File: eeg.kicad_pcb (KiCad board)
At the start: 2 copper layers, 155 parts, among them J1 USB_B_Mini, U1 STM32F446RE, U10 -.+2.5V.+3.3V-GND, U11 +5V, U12 RN4678-V_RM100, U13 ADS1299IPAG, U2 ADS1299-8CHANNEL, U3 LD39050PU33R, U4 TPS60403DBVT, U5 TPS73225DBVT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

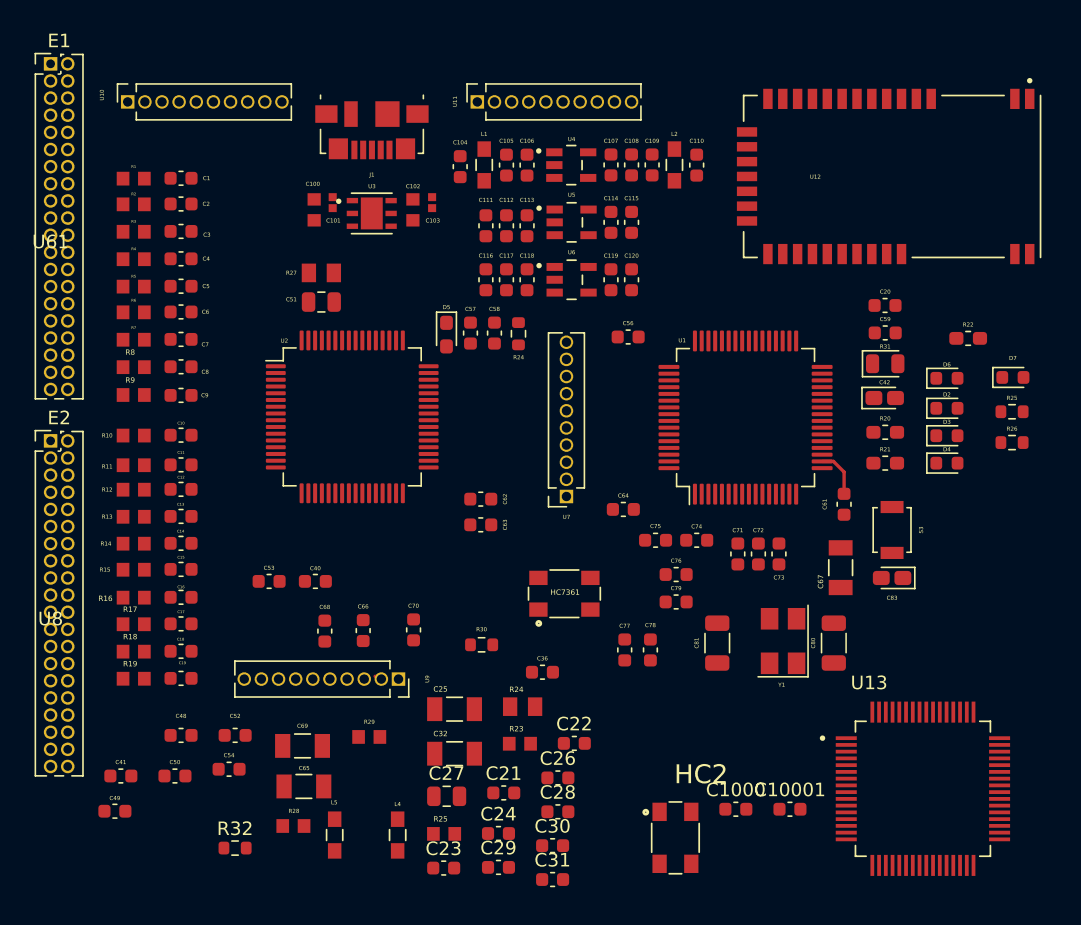
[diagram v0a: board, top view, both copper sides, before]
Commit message: RC connections realigned
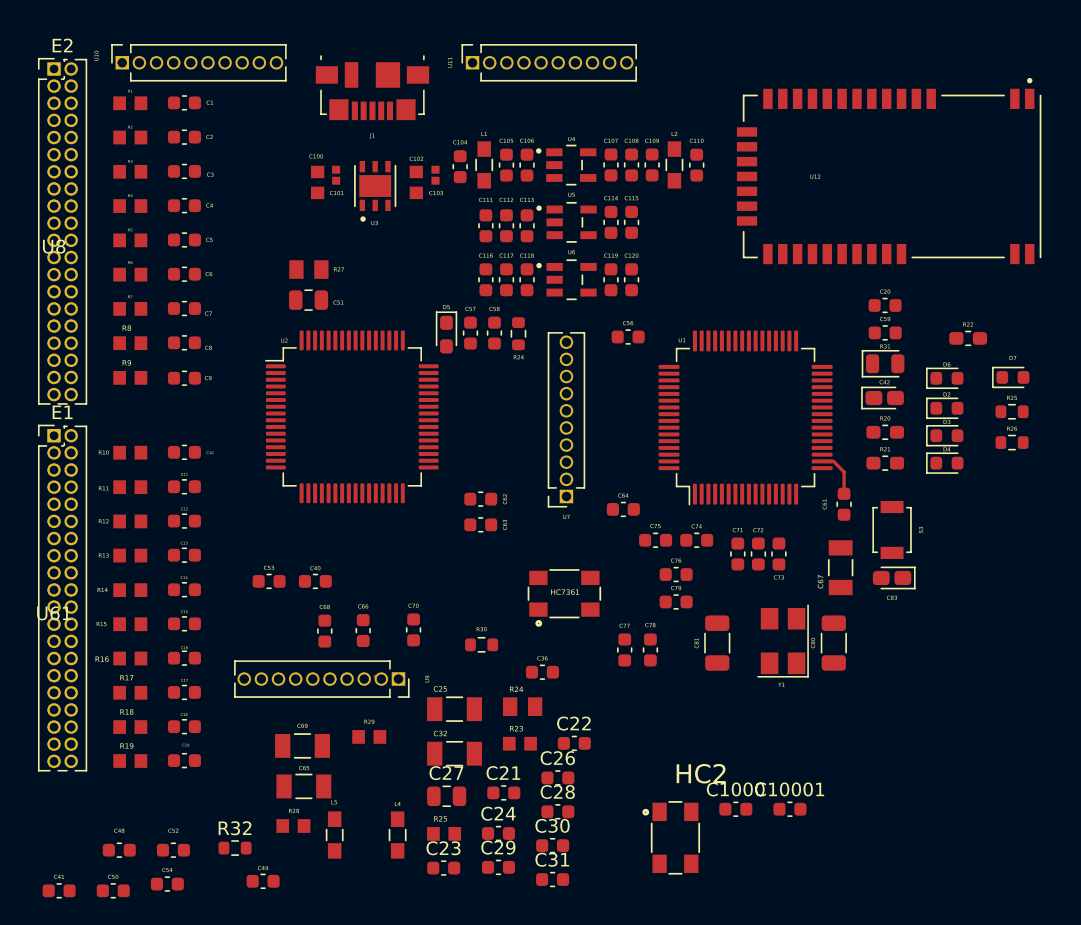
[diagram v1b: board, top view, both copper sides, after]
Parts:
- removed U13: ADS1299IPAG, QFP50P1200X1200X120-64N
- moved U61 27.6 mm to (39.8, 71.6)
- moved U8 27.6 mm to (39.8, 44.5)
- moved C49 12.1 mm to (55.2, 91.9)
- moved C50 9.66 mm to (44.1, 92.7)
- moved C52 9.66 mm to (48.6, 89.6)
- moved C54 9.66 mm to (48.2, 92.2)
- moved C41 9.66 mm to (40.1, 92.7)
- moved C48 9.66 mm to (44.6, 89.6)
- moved R19 6.10 mm to (45.4, 83.0)
- moved C19 6.10 mm to (49.4, 83.0)
- moved C1 5.59 mm to (49.4, 34.3)
- moved R1 5.59 mm to (45.4, 34.3)
- moved C18 5.59 mm to (49.4, 80.5)
- moved R18 5.59 mm to (45.4, 80.5)
- moved C17 5.09 mm to (49.4, 78.0)
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
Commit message: ADS1299 Tracks fixed.
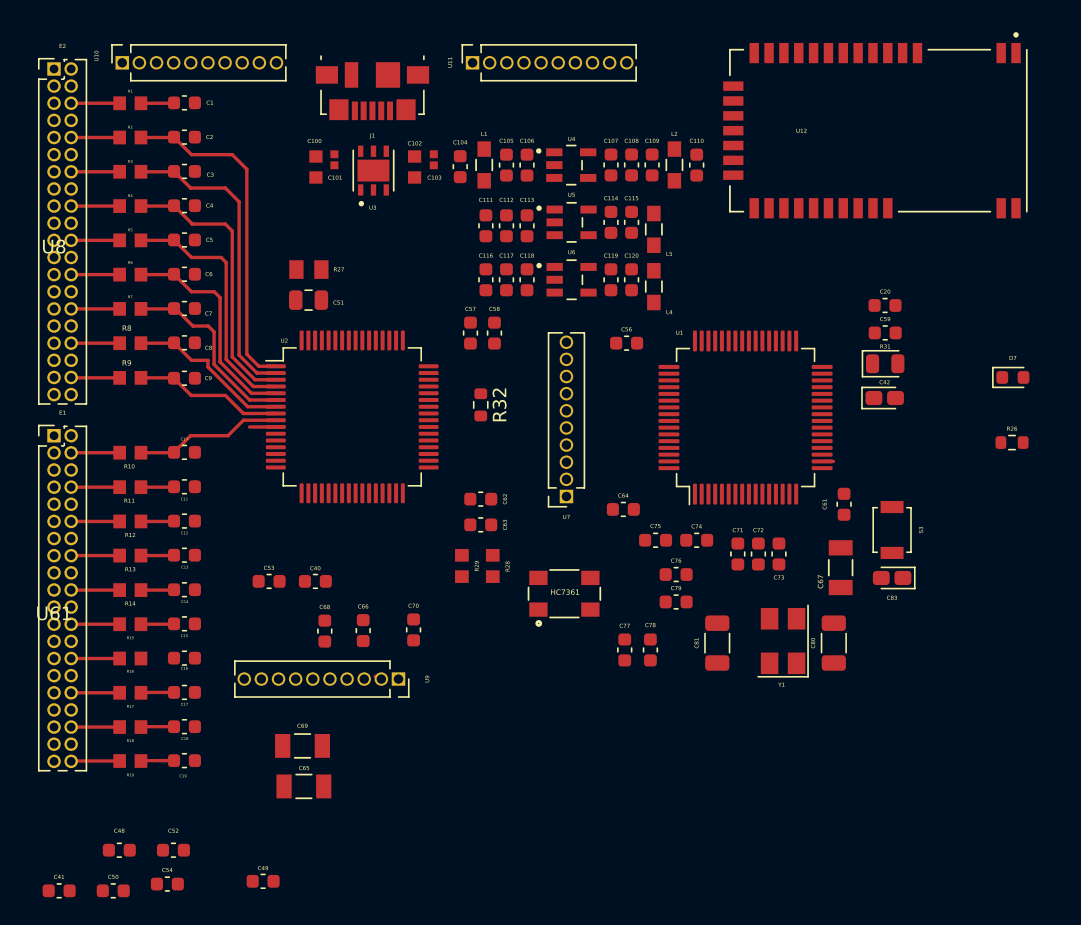
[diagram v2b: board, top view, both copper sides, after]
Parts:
- removed C1000, C23, C28, C29: 0.1uF, Capacitor_SMD:C_0603_1608Metric
- removed C10001, C22, C24, C26, C30, C31: 1uF, Capacitor_SMD:C_0603_1608Metric
- removed C21: 100uF, Capacitor_SMD:C_0603_1608Metric
- removed C25: 10uF, TCA1C106M8R:RESC3216X65N
- removed C27: 1.5nF, Capacitor_SMD:C_0805_2012Metric
- removed C32: 100uF, TCA1C106M8R:RESC3216X65N
- removed C36: 10uF, Capacitor_SMD:C_0603_1608Metric
- removed D2, D3, D4, D6: LED, LED_SMD:LED_0603_1608Metric
- removed D5: LED, LED_SMD:LED_0603_1608Metric_Pad1.05x0.95mm_HandSolder
- removed HC2: 2.048mhz, ERA-3A:OSCCC500X320X150N
- removed R20, R21: 270, Resistor_SMD:R_0603_1608Metric_Pad1.05x0.95mm_HandSolder
- removed R22: 100, Resistor_SMD:R_0603_1608Metric_Pad1.05x0.95mm_HandSolder
- removed R23, R25: 10K, ERA-3A:RESC1608X55N
- removed R24, R30: 100K, Resistor_SMD:R_0603_1608Metric
- removed R24: 1M, ERA-6AEB105V:RESC2012X60N
- removed R25: 10K, Resistor_SMD:R_0603_1608Metric
- moved L5 50.7 mm to (84.2, 43.6)
- moved L4 44.9 mm to (84.2, 47.9)
- moved R32 37.6 mm to (71.4, 56.6), turned to 270 degrees
- moved R28 24.3 mm to (72.3, 68.6), turned to 270 degrees
- moved R29 14.4 mm to (70.0, 68.6), turned to 270 degrees
- moved U12 3.54 mm to (100.8, 36.3)
- moved C100 1.15 mm to (59.2, 39.0)
- moved C101 1.15 mm to (60.5, 38.5)
- moved U3 1.15 mm to (63.4, 39.3)
- moved C102 1.15 mm to (66.5, 39.0)
- moved C103 1.15 mm to (67.9, 38.5)
- moved C56 0.47 mm to (82.2, 52.1)
- turned C10 to 180 degrees
- turned C11 to 180 degrees
- turned C12 to 180 degrees
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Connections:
- net Net-(U1-Pad20) renamed /NSS
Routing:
- net /IN8N: track 0.00 -> 25.1 mm
- net /IN8P: track 0.00 -> 22.9 mm
- net /IN7N: track 0.00 -> 20.8 mm
- net /IN7P: track 0.00 -> 18.7 mm
- net /IN6N: track 0.00 -> 16.5 mm
- net /IN6P: track 0.00 -> 14.2 mm
- net /IN5N: track 0.00 -> 12.3 mm
- net /IN5P: track 0.00 -> 11.1 mm
- net /IN4N: track 0.00 -> 11.0 mm
- net /IN4P: track 0.38 -> 4.41 mm
- net /CIN5P: track 0.00 -> 3.60 mm
- net /CSRB2: track 0.00 -> 3.60 mm
- net /CIN4N: track 0.00 -> 3.60 mm
- net /CIN2N: track 0.00 -> 3.60 mm
- net /CIN3P: track 0.00 -> 3.59 mm
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
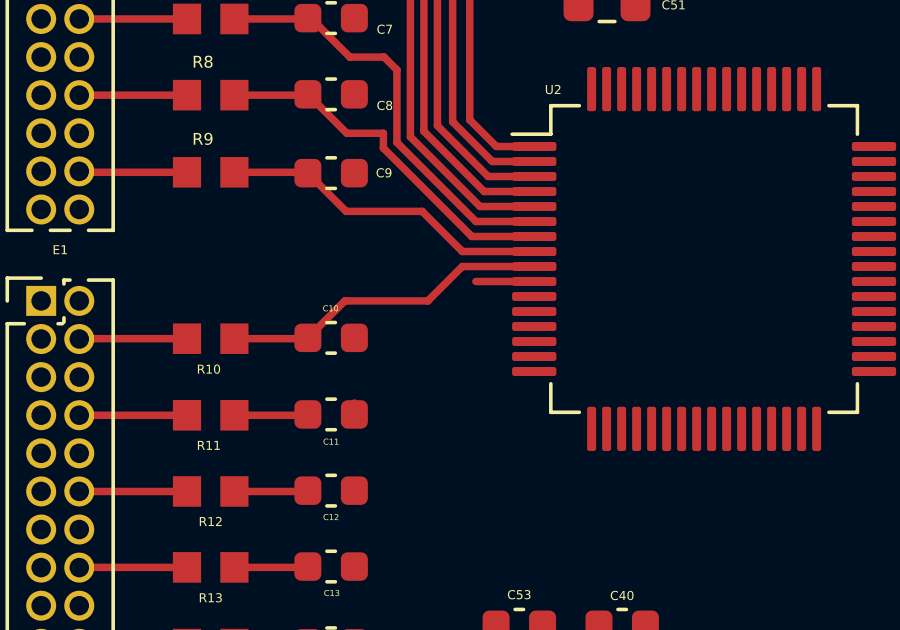
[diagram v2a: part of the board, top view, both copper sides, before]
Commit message: Electrode connections are completed
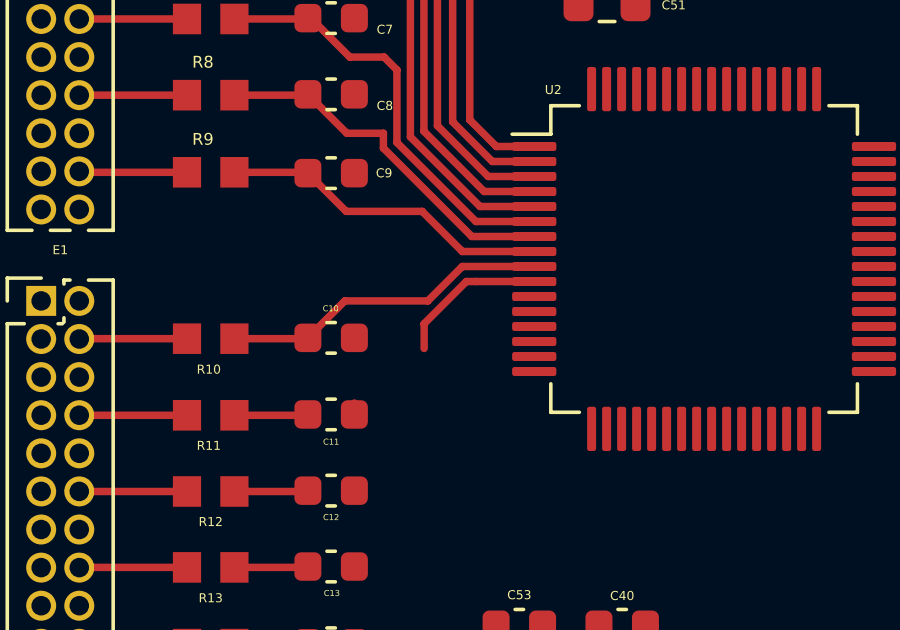
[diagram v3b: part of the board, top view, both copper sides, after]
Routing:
- net /IN4P: track 4.41 -> 7.54 mm

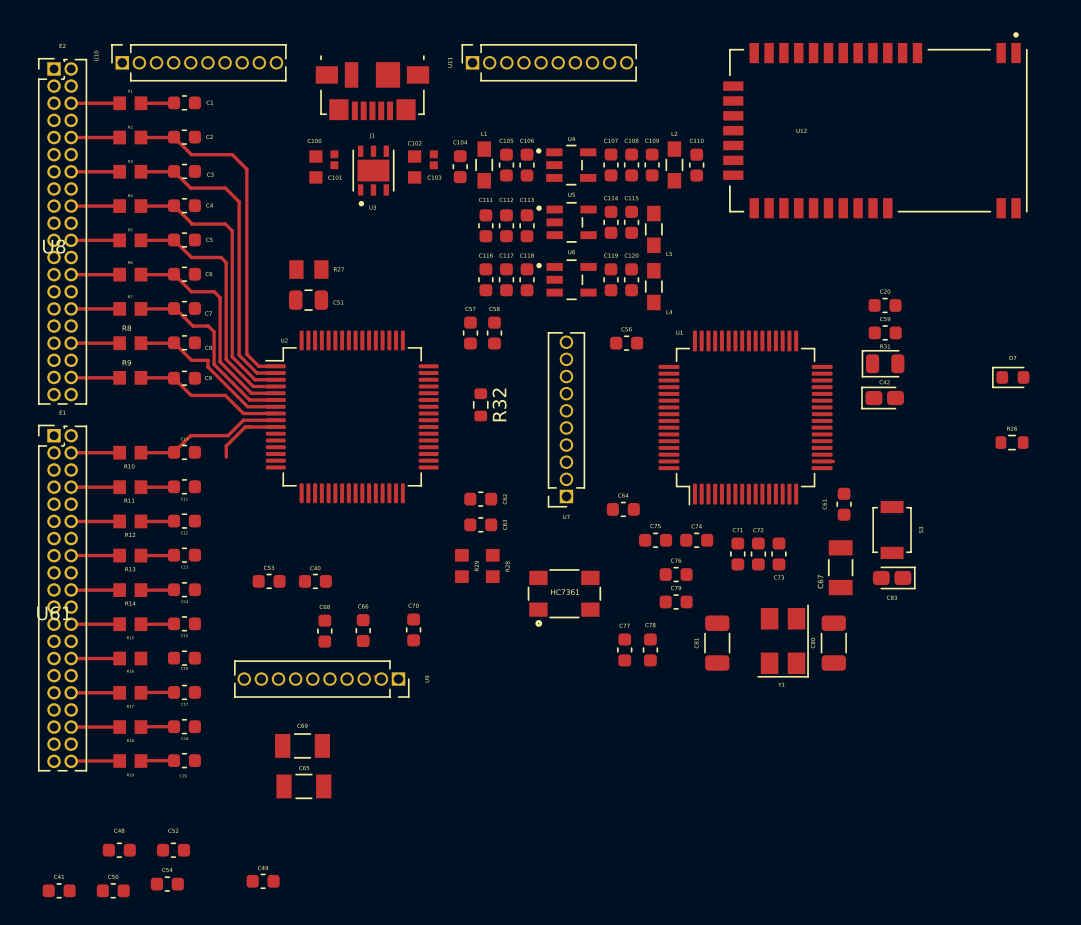
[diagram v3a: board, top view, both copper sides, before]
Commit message: VCAP capacitors are placed
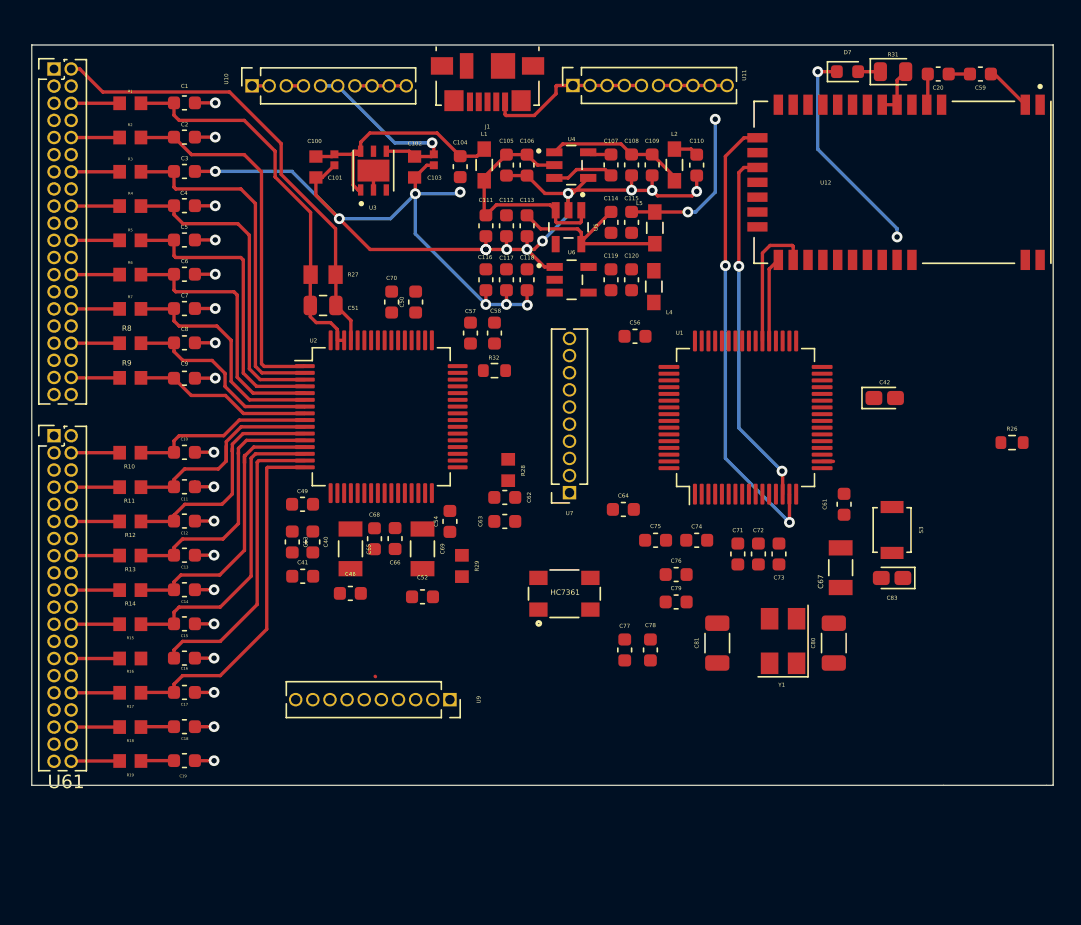
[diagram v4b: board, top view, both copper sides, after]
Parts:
- moved C50 49.0 mm to (66.5, 49.0), turned to 90 degrees
- moved C54 34.1 mm to (69.1, 65.3), turned to 90 degrees
- moved C41 29.5 mm to (58.2, 69.3)
- moved C49 28.1 mm to (58.2, 64.0)
- moved C52 26.3 mm to (67.1, 70.9)
- moved D7 25.8 mm to (98.5, 31.9)
- moved C48 25.6 mm to (61.7, 70.6)
- moved C70 24.3 mm to (64.8, 49.0)
- moved R31 21.7 mm to (101.9, 31.9)
- moved C59 20.4 mm to (108.4, 32.1), turned to 180 degrees
- moved C65 17.9 mm to (61.7, 67.3), turned to 270 degrees
- moved C20 17.6 mm to (105.3, 32.1), turned to 0 degrees
- moved C69 17.1 mm to (67.1, 67.3), turned to 270 degrees
- moved U10 9.77 mm to (54.4, 33.0)
- moved J1 8.55 mm to (71.9, 32.7)
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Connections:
- C1 pad 2: GND -> GNDA
- C10 pad 1: GND -> GNDA
- C100 pad 2: GND -> GNDA
- C101 pad 2: GND -> GNDA
- C102 pad 2: GND -> GNDA
- C103 pad 2: GND -> GNDA
- C104 pad 2: GND -> GNDA
- C105 pad 2: GND -> GNDA
- C106 pad 2: GND -> GNDA
- C108 pad 2: GND -> GNDA
- C109 pad 2: GND -> GNDA
- C11 pad 1: GND -> GNDA
- C110 pad 2: GND -> GNDA
- C111 pad 2: GND -> GNDA
- C112 pad 2: GND -> GNDA
- C113 pad 2: GND -> GNDA
- C114 pad 2: GND -> GNDA
- C115 pad 2: GND -> GNDA
- C116 pad 2: GND -> GNDA
- C117 pad 2: GND -> GNDA
- C118 pad 2: GND -> GNDA
- C119 pad 2: GND -> GNDA
- C12 pad 1: GND -> GNDA
- C120 pad 2: GND -> GNDA
- C13 pad 1: GND -> GNDA
- C14 pad 1: GND -> GNDA
- C15 pad 1: GND -> GNDA
- C16 pad 1: GND -> GNDA
- C17 pad 1: GND -> GNDA
- C18 pad 1: GND -> GNDA
- C19 pad 1: GND -> GNDA
- C2 pad 2: GND -> GNDA
- C3 pad 1: GND -> GNDA
- C4 pad 2: GND -> GNDA
- C40 pad 2: GND -> GNDA
- C41 pad 2: GND -> GNDA
- C48 pad 1: GND -> GNDA
- C49 pad 2: GND -> GNDA
- C5 pad 1: GND -> GNDA
- C52 pad 1: GND -> GNDA
- C53 pad 2: GND -> GNDA
- C6 pad 2: GND -> GNDA
- C62 pad 1: GND -> GNDA
- C63 pad 1: GND -> GNDA
- C7 pad 1: GND -> GNDA
- C8 pad 2: GND -> GNDA
- C9 pad 1: GND -> GNDA
- U3 pad 2: GND -> GNDA
- U3 pad 7: GND -> GNDA
- U4 pad 4: GND -> GNDA
- U5 pad 2: GND -> GNDA
- U6 pad 1: GND -> GNDA
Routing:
- net GNDA: track 0.00 -> 123.1 mm, vias 0 -> 34
- net /BIASINV: track 0.00 -> 34.6 mm
- net /RN46CTS: track 0.00 -> 34.1 mm, vias 0 -> 2
- net +5V: track 0.00 -> 30.5 mm
- net /RN46RTS: track 0.00 -> 26.7 mm, vias 0 -> 2
- net /BIASIN: track 2.46 -> 29.0 mm
- net /IN1P: track 2.46 -> 26.4 mm
- net /IN1N: track 0.00 -> 22.3 mm
- net /IN2P: track 2.46 -> 23.0 mm
- net /IN2N: track 2.46 -> 21.5 mm
- net Net-(C105-Pad1): track 0.00 -> 18.4 mm
- net /IN3P: track 2.46 -> 19.4 mm
- net +3V3: track 0.38 -> 16.6 mm, vias 0 -> 1
- net Net-(D7-Pad1): track 0.00 -> 16.1 mm, vias 0 -> 2
- net /IN3N: track 2.46 -> 17.5 mm
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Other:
- board outline added: 75.7 x 54.9 mm
